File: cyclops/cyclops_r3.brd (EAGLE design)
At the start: 124.5 x 79.9 mm, 136 parts, among them Q1 BC817, Q2 IRF510, U1 MCP4921, U10 TLV2374, U11 THS4281, U12 MAX4564, U13 ZXTD, U14 ZXTD, U2 ADG3301, U3 MCP4022-50k, U4 LT1931, U5 LT1764A, U6 337L, U7 TLV3701, U8 ADR03, U9 OP1177, X1 SLP3, X2 SLP3, X3 SLP3

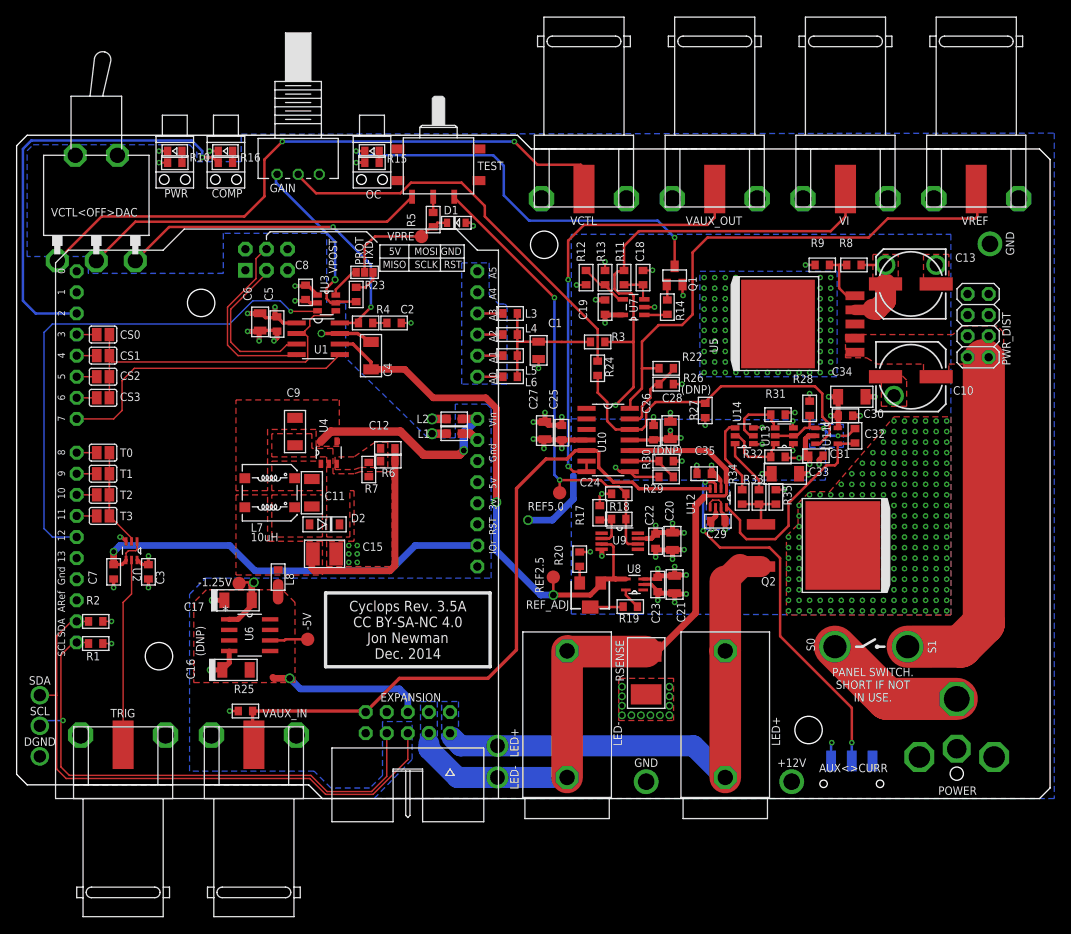
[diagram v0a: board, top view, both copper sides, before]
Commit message: A few changes made to comply with CircuitHub stuff
- Almost ready to do a circuit hub run.
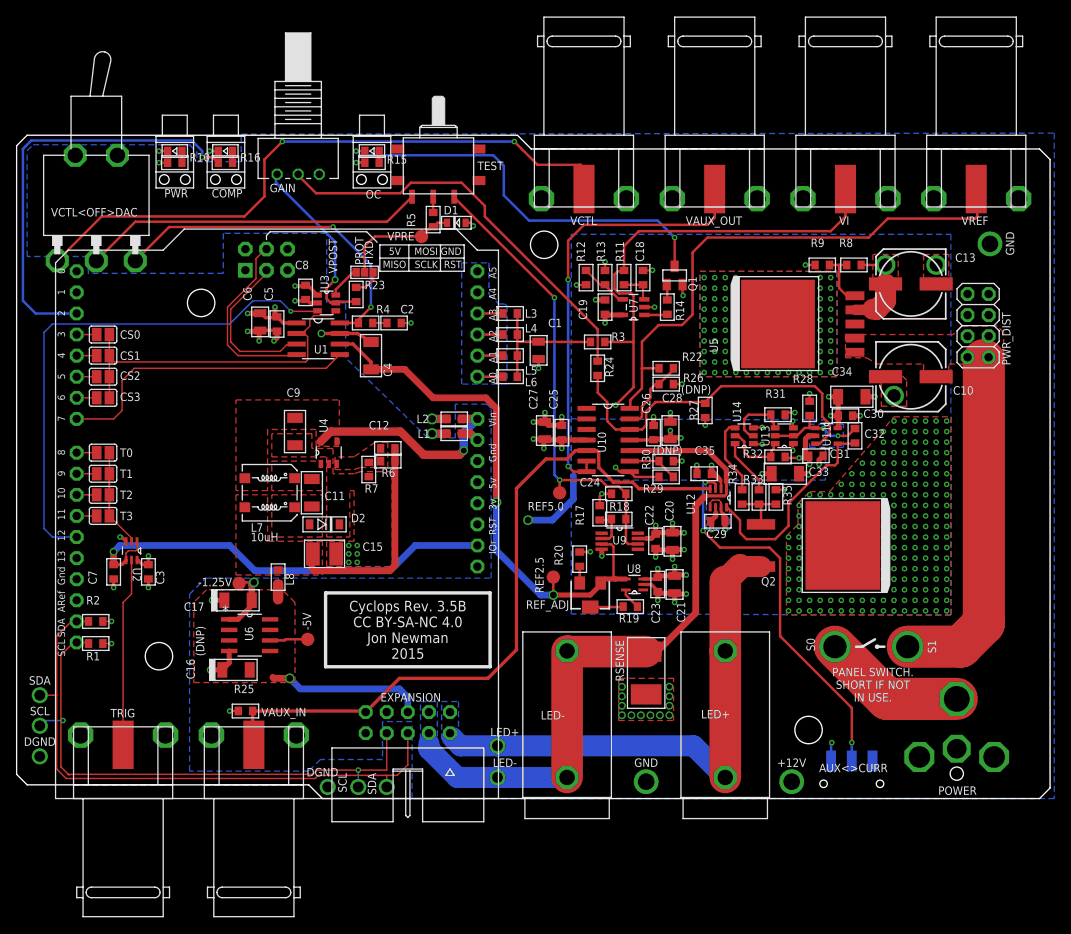
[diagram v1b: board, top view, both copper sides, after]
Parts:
- COMP: value ORG -> RED
- LED+: value A2107-R -> 24.243.1
- LED-: value A2107-B -> 24.243.2
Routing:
- net GND: track 117.8 -> 143.6 mm, vias 136 -> 137
- net SDA: track 71.1 -> 71.3 mm, vias 1 -> 2
- net SCL: track 67.2 -> 67.3 mm, vias 2 -> 4
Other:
- board text added: "CC BY-SA-NC 4.0 Jon Newman 2015"
- board text added: "Cyclops Rev. 3.5B"
- board text added: "Cyclops Rev. 3.5B CC BY-SA-NC 4.0 Jon Newman 2015"
- board text removed: "CC BY-SA-NC 4.0 Jon Newman Dec. 2014"
- board text removed: "Cyclops Rev. 3.5A"
- board text removed: "Cyclops Rev. 3.5A CC BY-SA-NC 4.0 Jon Newman Dec. 2014"

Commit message: Reworked overcurrent circuit.
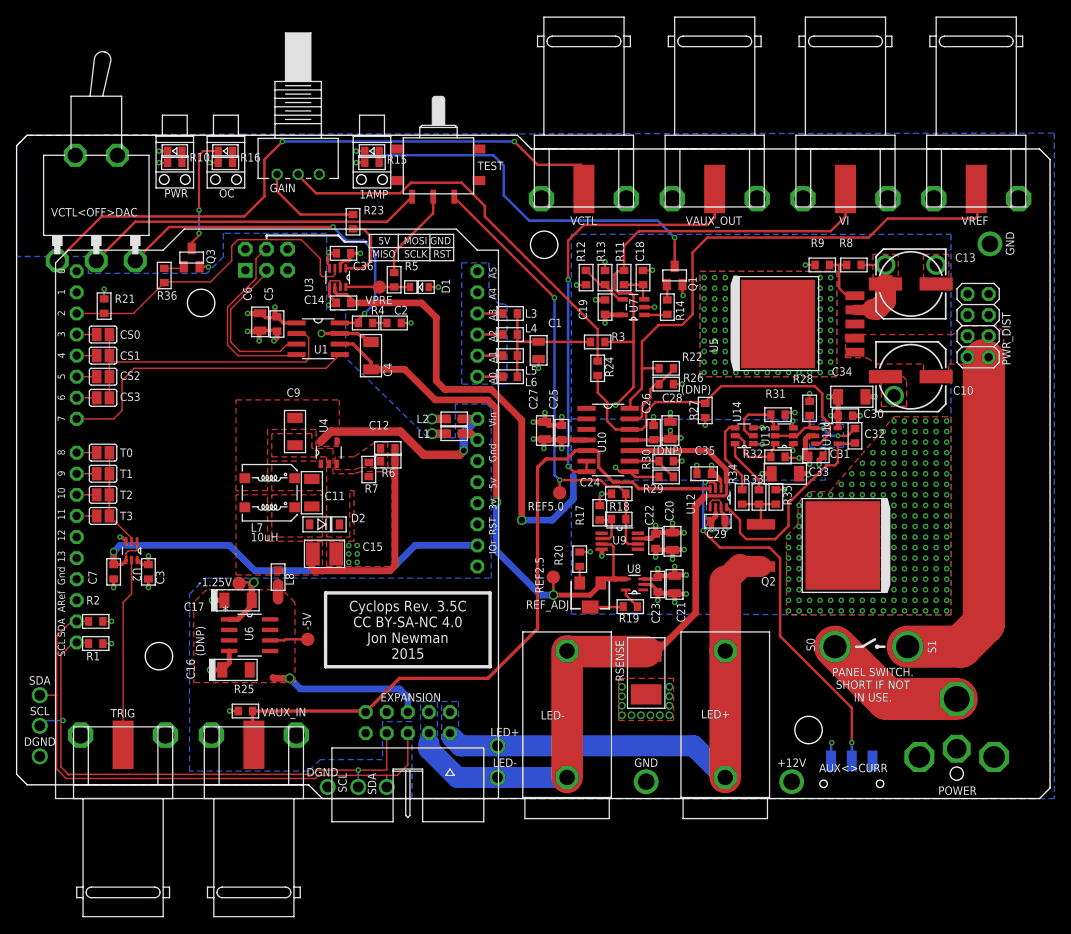
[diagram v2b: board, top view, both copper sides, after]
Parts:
- removed C8: .1uF, cyclops:0603
- removed COMP: RED, cyclops:LED-0603
- removed SJ1: (no value), jonnew:SJ_2_0603
- added 1AMP: RED, cyclops:LED-0603
- added C14, C36: 10nF, cyclops:0603
- added Q3: BC817, cyclops:SOT23-BEC
- added R21, R36: 10k, cyclops:0603
- R16: value 470 -> 1k
- U3: value MCP4022-50k -> MAX4564; device cyclops:SOT23-6 -> cyclops:SOT65P300X175-N
- moved OC 17.7 mm to (26.4, 78.0)
- moved D1 8.93 mm to (48.5, 61.6)
- moved R23 8.77 mm to (40.5, 69.5), turned to 270 degrees
- moved R5 8.63 mm to (45.5, 62.5)
- moved VPRE 7.94 mm to (43.7, 61.6)
- moved U3 3.47 mm to (39.0, 62.7)
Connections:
- removed net OC_COMP: LEONARDO.D2, R16.2
- removed net POT: LEONARDO.D12, U3.3
- removed net VCTL_FIXED: R23.2, SJ1.1
- new net N$39: Q3.B, R36.1
- new net OVER_CURR: LEONARDO.D2, R21.1, R36.2, U3.3
- new net VCTL_PROT: R23.2, U3.1
- net +12V: now also C36.1, R16.2, U3.2
- net +5V: no longer C8.1, U3.1
- net -1.25V: now also C14.1, U3.6
- net CS: no longer U3.4
- net GND: now also C14.2, C36.2, Q3.E, R21.2, U3.4, U3.5, U3.7; no longer C8.2, COMP.C, U3.2
- net N$16: now also OC.A; no longer COMP.A
- net N$2: now also 1AMP.A; no longer OC.A
- net N$38: now also OC.C, Q3.C; no longer SJ1.2, U3.6
- net N$9: now also 1AMP.C; no longer OC.C
- net VCTL: now also U3.8; no longer SJ1.COM
- net VCTL_PROTECT: no longer U3.5
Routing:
- net POT: track 63.0 -> 0.00 mm, vias 1 -> 0
- net OC_COMP: track 50.9 -> 0.00 mm, vias 1 -> 0
- net -1.25V: track 79.3 -> 125.7 mm
- net OVER_CURR: track 0.00 -> 39.7 mm
- net GND: track 143.6 -> 113.2 mm, vias 137 -> 139
- net N$38: track 4.00 -> 14.1 mm, vias 0 -> 2
- net VCTL_PROTECT: track 22.2 -> 12.3 mm, vias 1 -> 0
- net N$14: track 2.40 -> 11.3 mm
- net VCTL_PROT: track 0.00 -> 8.86 mm
- net VCTL: track 14.5 -> 7.78 mm
- net CS: track 42.2 -> 36.8 mm
- net +12V: track 57.4 -> 62.3 mm, vias 206 -> 208
- net VCTL_FIXED: track 3.30 -> 0.00 mm
- net +5V: track 15.6 -> 12.4 mm, vias 6 -> 5
- net N$39: track 0.00 -> 2.43 mm
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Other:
- board text added: "Cyclops Rev. 3.5C"
- board text added: "Cyclops Rev. 3.5C CC BY-SA-NC 4.0 Jon Newman 2015"
- board text removed: "Cyclops Rev. 3.5B"
- board text removed: "Cyclops Rev. 3.5B CC BY-SA-NC 4.0 Jon Newman 2015"
- board text removed: "FIXD"
- board text removed: "PROT"
- board text removed: "VPOST"

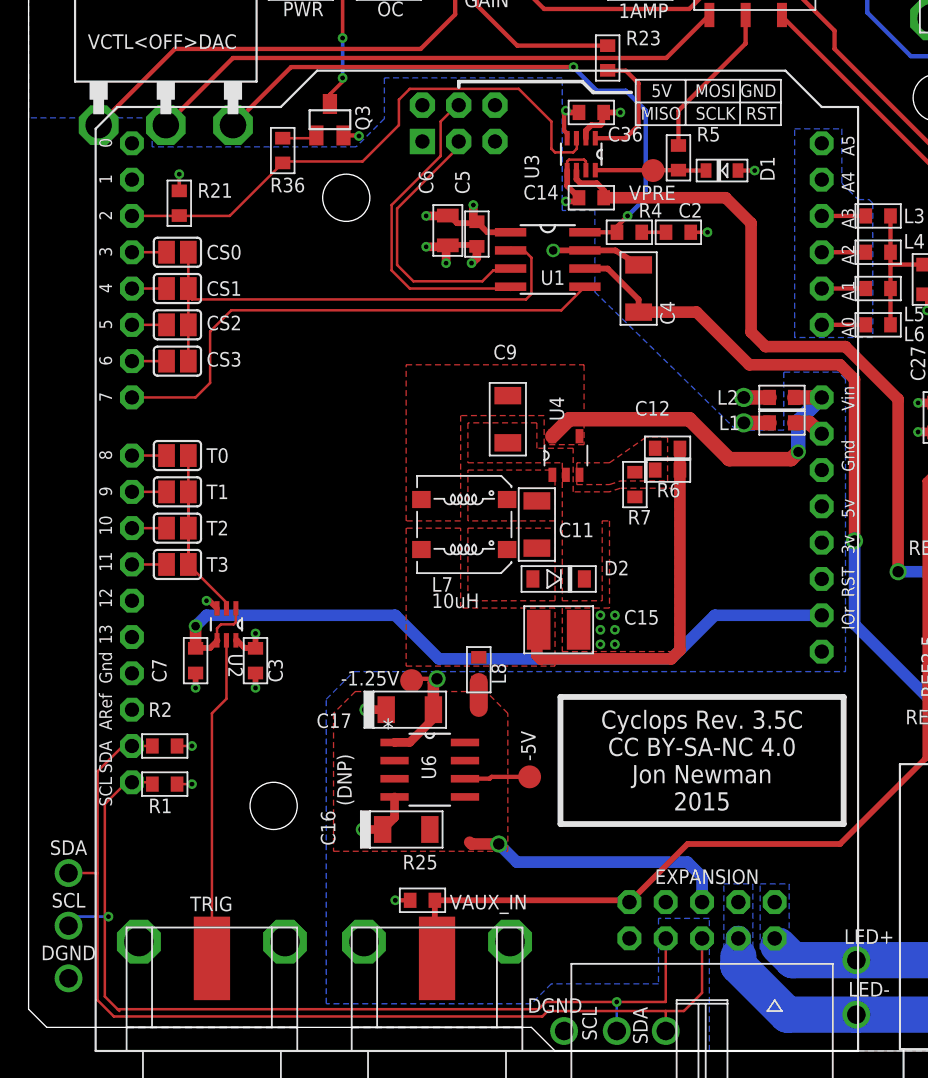
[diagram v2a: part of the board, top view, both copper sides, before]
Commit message: Further improvements to overcurrent circuitry.
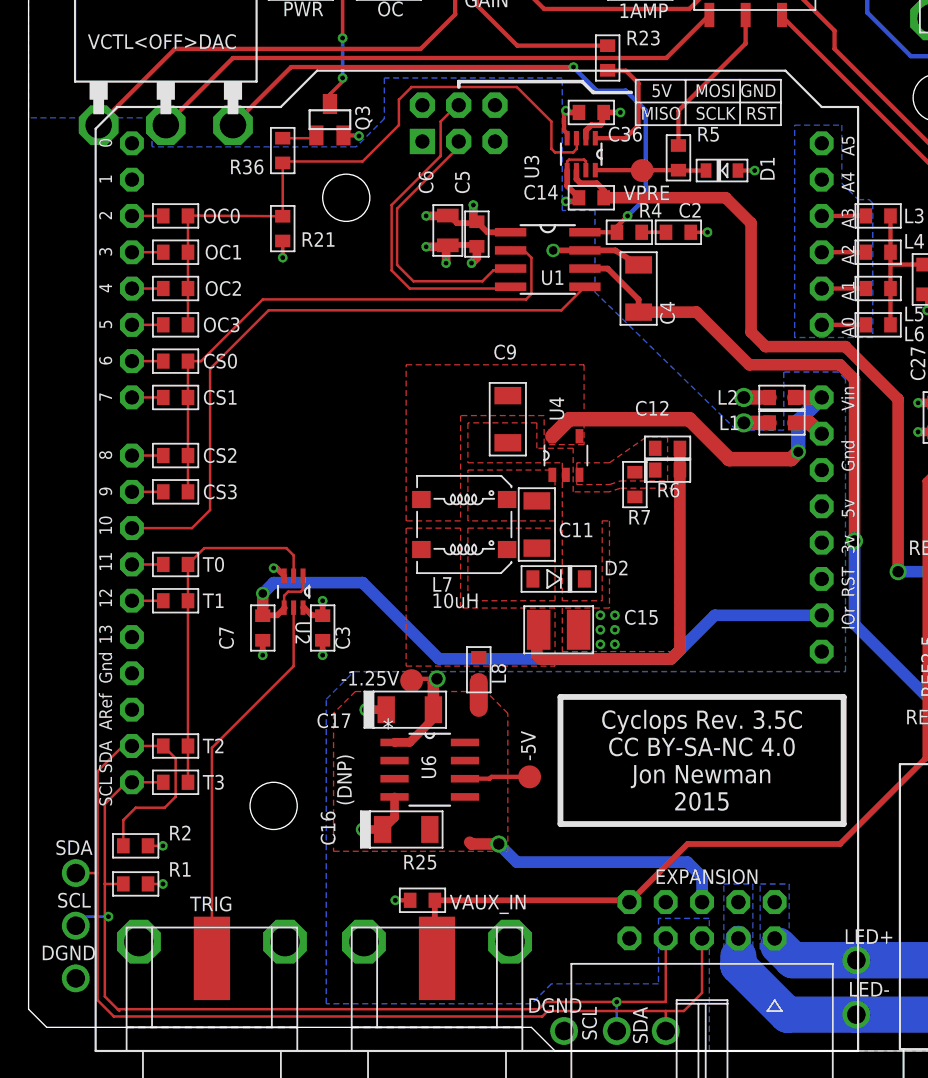
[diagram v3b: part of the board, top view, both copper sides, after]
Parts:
- added OC0, OC1, OC2, OC3: 0, cyclops:0603
- CS0, CS1, CS2, CS3, T0, T1, T2, T3: value (none) -> 0; device cyclops:SJ -> cyclops:0603
- R5: value 120 -> 100
- moved T2 15.2 mm to (10.3, 21.3), turned to 0 degrees
- moved T3 15.2 mm to (10.3, 18.8), turned to 0 degrees
- moved CS2 9.14 mm to (10.3, 41.7), turned to 180 degrees
- moved CS3 9.14 mm to (10.3, 39.1), turned to 180 degrees
- moved CS0 7.62 mm to (10.3, 48.3), turned to 180 degrees
- moved CS1 7.62 mm to (10.3, 45.7), turned to 180 degrees
- moved T1 7.62 mm to (10.3, 31.5), turned to 0 degrees
- moved T0 7.62 mm to (10.3, 34.0), turned to 0 degrees
- moved R21 7.45 mm to (17.8, 57.5), turned to 270 degrees
- moved R1 7.27 mm to (7.49, 11.7)
- moved R2 7.27 mm to (7.49, 14.4)
- moved C3 5.23 mm to (20.6, 29.6)
- moved U2 5.23 mm to (18.5, 32.1)
- moved C7 5.23 mm to (16.4, 29.6)
- moved VPRE 0.76 mm to (42.9, 61.6)
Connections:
- removed net SCL: EXPANSION.8, LEONARDO.SCL, R1.2
- removed net SDA: EXPANSION.6, LEONARDO.SDA, R2.2
- removed net T2: LEONARDO.D10, T2.2
- removed net T3: LEONARDO.D11, T3.2
- new net N$40: LEONARDO.D2, OC0.2
- new net OC0: LEONARDO.D3, OC1.2
- new net OC1: LEONARDO.D4, OC2.2
- new net OC2: LEONARDO.D5, OC3.2
- new net SCL/T3: EXPANSION.8, LEONARDO.SCL, R1.2, T3.1
- new net SDA/T2: EXPANSION.6, LEONARDO.SDA, R2.2, T2.1
- net CS: now also CS0.1, CS1.1, CS2.1, CS3.1; no longer CS0.2, CS1.2, CS2.2, CS3.2
- net CS0: now also CS0.2, LEONARDO.D6; no longer CS0.1, LEONARDO.D3
- net CS1: now also CS1.2, LEONARDO.D7; no longer CS1.1, LEONARDO.D4
- net CS2: now also CS2.2, LEONARDO.D8; no longer CS2.1, LEONARDO.D5
- net CS3: now also CS3.2, LEONARDO.D9; no longer CS3.1, LEONARDO.D6
- net LDAC: now also LEONARDO.D10; no longer LEONARDO.D7
- net OVER_CURR: now also OC0.1, OC1.1, OC2.1, OC3.1; no longer LEONARDO.D2
- net T0: now also LEONARDO.D11, T0.1; no longer LEONARDO.D8, T0.2
- net T1: now also LEONARDO.D12, T1.1; no longer LEONARDO.D9, T1.2
- net TRIG: now also T0.2, T1.2, T2.2, T3.2; no longer T0.1, T1.1, T2.1, T3.1
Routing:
- net SDA/T2: track 0.00 -> 81.6 mm, vias 0 -> 2
- net SDA: track 71.3 -> 0.00 mm, vias 2 -> 0
- net SCL/T3: track 0.00 -> 68.8 mm, vias 0 -> 4
- net SCL: track 67.3 -> 0.00 mm, vias 4 -> 0
- net TRIG: track 16.9 -> 25.1 mm
- net LDAC: track 37.0 -> 44.5 mm
- net OVER_CURR: track 39.7 -> 45.8 mm
- net TRIG_EXT: track 22.7 -> 26.9 mm
- net VLOGIC: track 53.3 -> 49.5 mm
- net CS: track 36.8 -> 39.6 mm
- net T3: track 2.42 -> 0.00 mm
- net T2: track 2.42 -> 0.00 mm
- net OC2: track 0.00 -> 2.19 mm
- net OC1: track 0.00 -> 2.19 mm
- net OC0: track 0.00 -> 2.19 mm
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
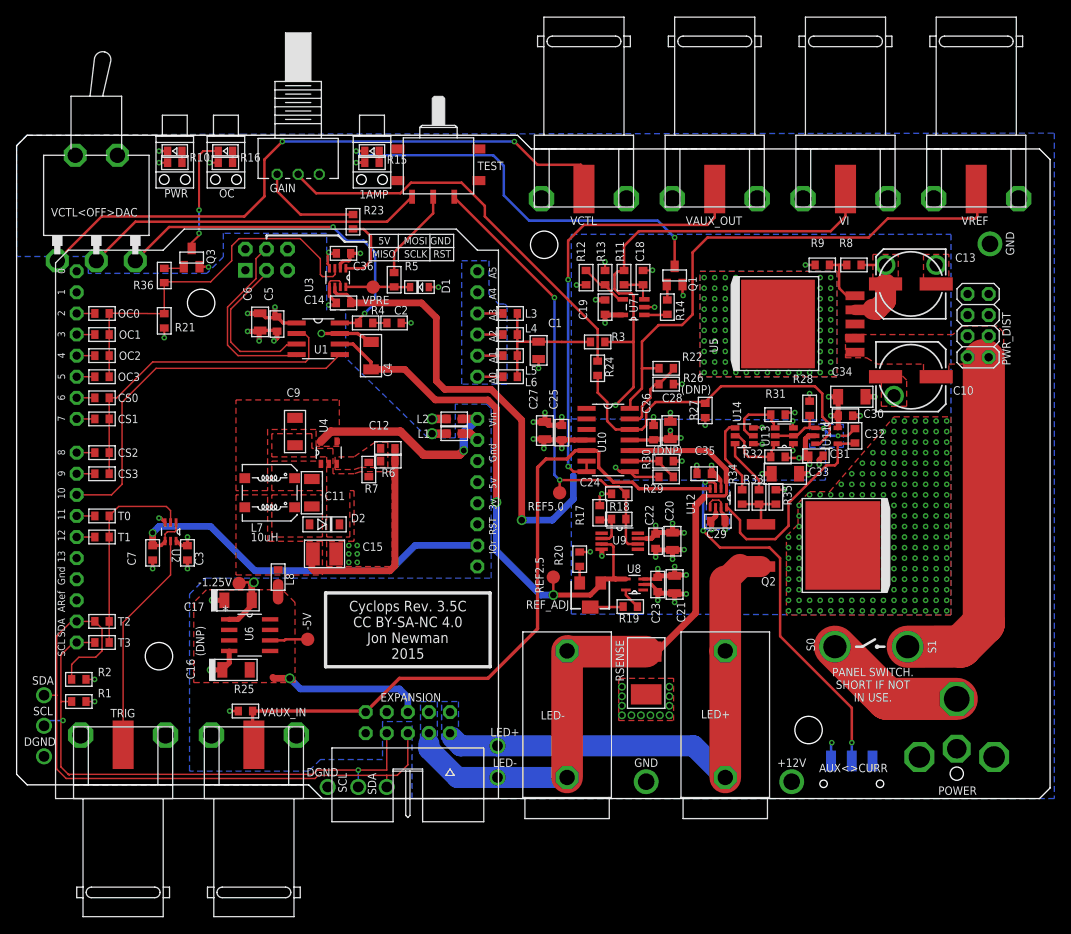
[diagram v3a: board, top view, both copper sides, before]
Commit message: Addeda jumper to bypass the oc switch circuit.
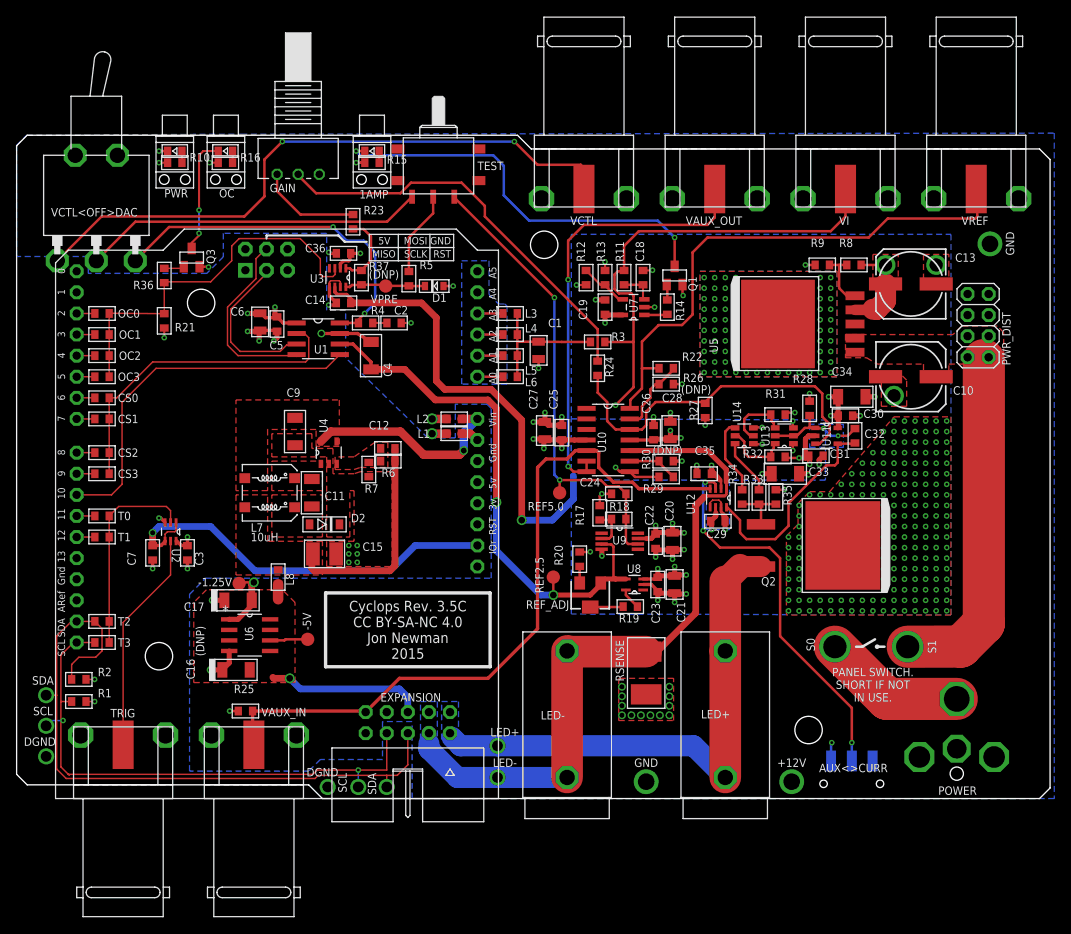
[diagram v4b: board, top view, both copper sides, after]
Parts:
- added R37: 0, cyclops:0603
- moved D1 1.78 mm to (50.3, 61.7)
- moved R5 1.78 mm to (47.2, 62.6)
- moved VPRE 1.53 mm to (44.5, 61.7)
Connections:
- net GND: no longer U3.4
- net VCTL: now also R37.2
- net VCTL_PROT: now also R37.1
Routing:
- net GND: track 113.2 -> 111.3 mm
- net N$14: track 11.3 -> 10.5 mm
- net VCTL: track 9.23 -> 9.74 mm
